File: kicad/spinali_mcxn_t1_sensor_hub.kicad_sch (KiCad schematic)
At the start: 0 parts

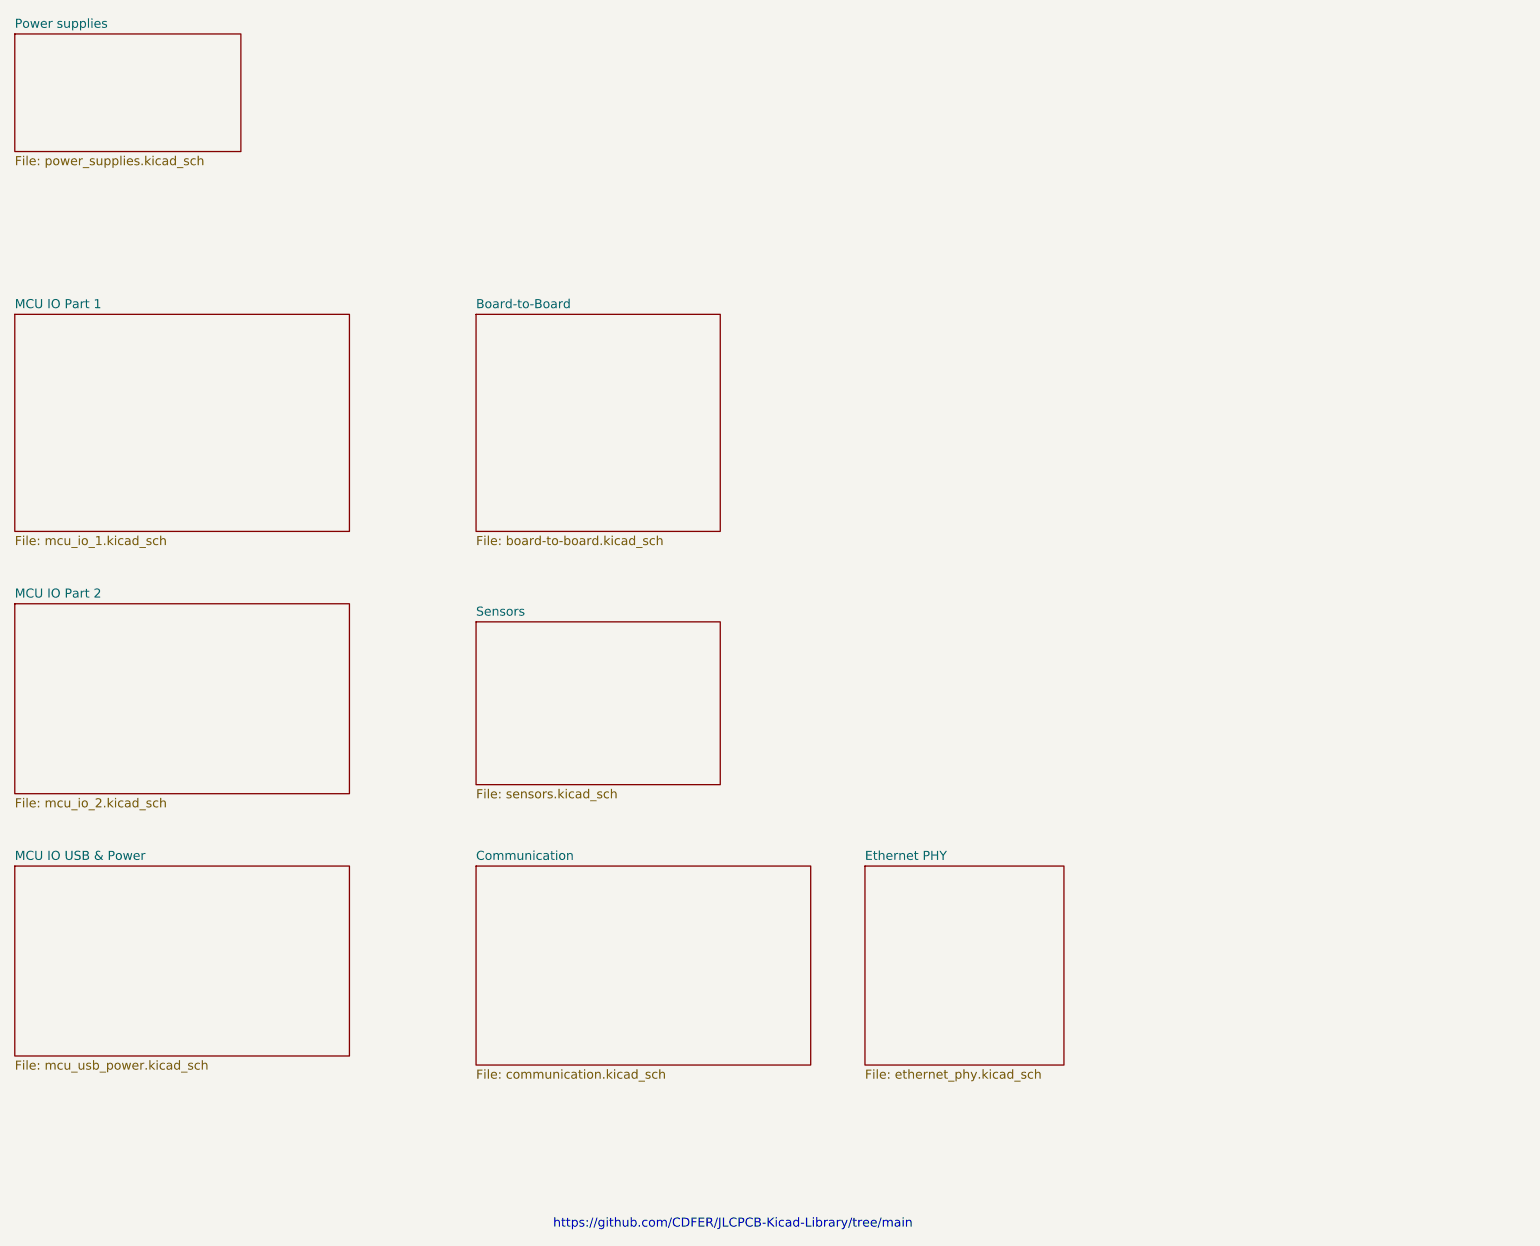
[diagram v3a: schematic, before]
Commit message: Updated schematic after feedback from Jari
- Finished schematic after feedback from Jari. It is at a finished state, can be reviewed by whole team now.
- Layouted MCXN with decoupling caps.
- Layouted Base100-T1 ethernet phy.
- Layouted the power supply a bit.
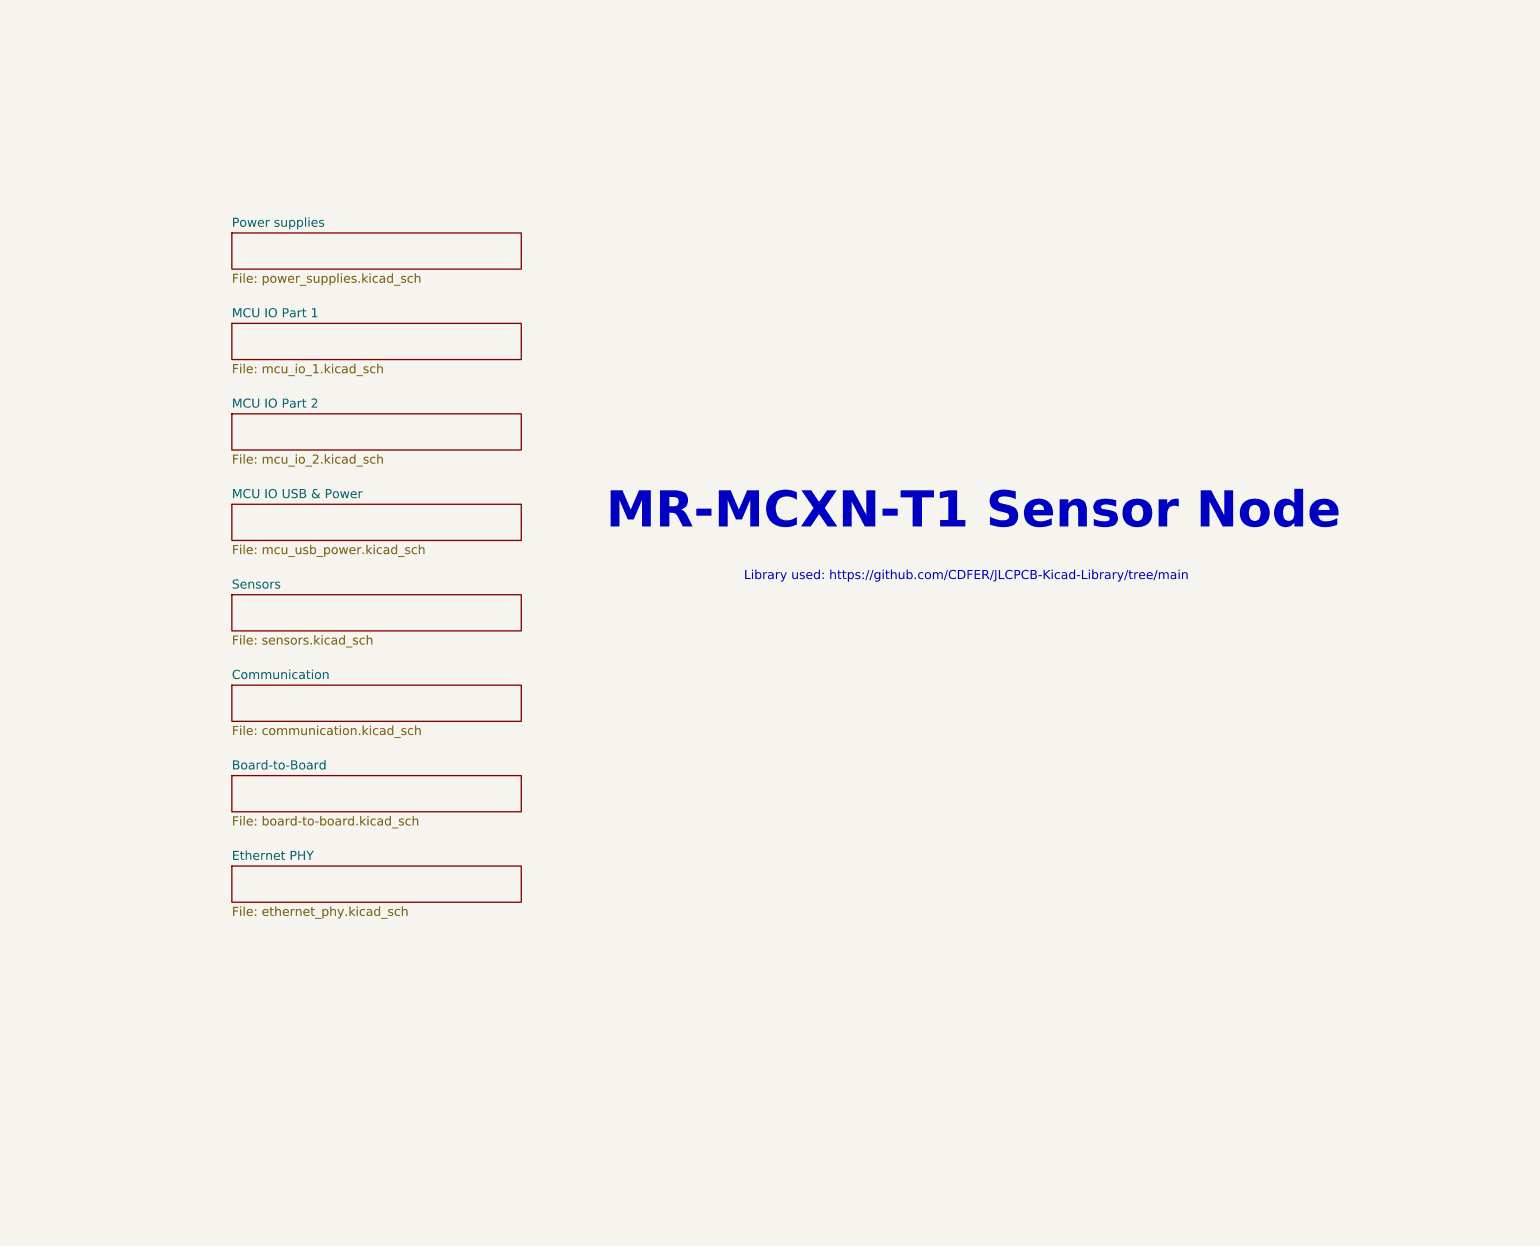
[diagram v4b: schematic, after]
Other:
- note added: "Library used: https://github.com/CDFER/JLCPCB-Kicad-Library/tree/main"
- note added: "MR-MCXN-T1 Sensor Node"
- note removed: "https://github.com/CDFER/JLCPCB-Kicad-Library/tree/main"
- title: MR-MCXN-T1 Sensor hub -> MR-MCXN-T1 Sensor Node
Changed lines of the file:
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@@
 	(paper "A4")
 	(title_block
-		(title "MR-MCXN-T1 Sensor hub")
-		(date "2025-03-20")
+		(title "MR-MCXN-T1 Sensor Node")
+		(date "2025-03-28")
 		(rev "X0")
 		(company "NXP SEMICONDUCTORS B.V.")
@@
 		(comment 4 "CTO SYSTEM INNOVATIONS / MOBILE ROBOTICS DOMAIN")
 	)
-	(text "https://github.com/CDFER/JLCPCB-Kicad-Library/tree/main"
+	(text "MR-MCXN-T1 Sensor Node"
 		(exclude_from_sim no)
-		(at 121.158 191.262 0)
+		(at 154.94 91.186 0)
+		(effects
+			(font
+				(size 5.08 5.08)
+				(thickness 1.016)
+				(bold yes)
+			)
+		)
+	)
+	(text "Library used: https://github.com/CDFER/JLCPCB-Kicad-Library/tree/main"
+		(exclude_from_sim no)
+		(at 153.924 100.33 0)
 		(effects
 			(font
@@
 	)
 	(sheet
-		(at 85.09 63.5)
-		(size 34.29 30.48)
+		(at 50.8 128.27)
+		(size 40.64 5.08)
 		(fields_autoplaced yes)
 		(stroke
@@
 		)
 		(property "Sheetname" "Board-to-Board"
-			(at 85.09 62.7884 0)
+			(at 50.8 127.5584 0)
 			(effects
 				(font
@@
 		)
 		(property "Sheetfile" "board-to-board.kicad_sch"
-			(at 85.09 94.5646 0)
+			(at 50.8 133.9346 0)
 			(effects
 				(font
@@
 	)
 	(sheet
-		(at 20.32 63.5)
-		(size 46.99 30.48)
+		(at 50.8 64.77)
+		(size 40.64 5.08)
 		(fields_autoplaced yes)
 		(stroke
@@
 		)
 		(property "Sheetname" "MCU IO Part 1"
-			(at 20.32 62.7884 0)
+			(at 50.8 64.0584 0)
 			(effects
 				(font
@@
 		)
 		(property "Sheetfile" "mcu_io_1.kicad_sch"
-			(at 20.32 94.5646 0)
+			(at 50.8 70.4346 0)
 			(effects
 				(font
@@
 	)
 	(sheet
-		(at 20.32 104.14)
-		(size 46.99 26.67)
+		(at 50.8 77.47)
+		(size 40.64 5.08)
 		(fields_autoplaced yes)
 		(stroke
@@
 		)
 		(property "Sheetname" "MCU IO Part 2"
-			(at 20.32 103.4284 0)
+			(at 50.8 76.7584 0)
 			(effects
 				(font
@@
 		)
 		(property "Sheetfile" "mcu_io_2.kicad_sch"
-			(at 20.32 131.3946 0)
+			(at 50.8 83.1346 0)
 			(effects
 				(font
@@
 	)
 	(sheet
-		(at 139.7 140.97)
-		(size 27.94 27.94)
+		(at 50.8 140.97)
+		(size 40.64 5.08)
 		(fields_autoplaced yes)
 		(stroke
@@
 		)
 		(property "Sheetname" "Ethernet PHY"
-			(at 139.7 140.2584 0)
+			(at 50.8 140.2584 0)
 			(effects
 				(font
@@
 		)
 		(property "Sheetfile" "ethernet_phy.kicad_sch"
-			(at 139.7 169.4946 0)
+			(at 50.8 146.6346 0)
 			(effects
 				(font
@@
 	)
 	(sheet
-		(at 85.09 106.68)
-		(size 34.29 22.86)
+		(at 50.8 102.87)
+		(size 40.64 5.08)
 		(fields_autoplaced yes)
 		(stroke
@@
 		)
 		(property "Sheetname" "Sensors"
-			(at 85.09 105.9684 0)
+			(at 50.8 102.1584 0)
 			(effects
 				(font
@@
 		)
 		(property "Sheetfile" "sensors.kicad_sch"
-			(at 85.09 130.1246 0)
+			(at 50.8 108.5346 0)
 			(effects
 				(font
@@
 	)
 	(sheet
-		(at 85.09 140.97)
-		(size 46.99 27.94)
+		(at 50.8 115.57)
+		(size 40.64 5.08)
 		(fields_autoplaced yes)
 		(stroke
@@
 		)
 		(property "Sheetname" "Communication"
-			(at 85.09 140.2584 0)
+			(at 50.8 114.8584 0)
 			(effects
 				(font
@@
 		)
 		(property "Sheetfile" "communication.kicad_sch"
-			(at 85.09 169.4946 0)
+			(at 50.8 121.2346 0)
 			(effects
 				(font
@@
 	)
 	(sheet
-		(at 20.32 140.97)
-		(size 46.99 26.67)
+		(at 50.8 90.17)
+		(size 40.64 5.08)
 		(fields_autoplaced yes)
 		(stroke
@@
 		)
 		(property "Sheetname" "MCU IO USB & Power"
-			(at 20.32 140.2584 0)
+			(at 50.8 89.4584 0)
 			(effects
 				(font
@@
 		)
 		(property "Sheetfile" "mcu_usb_power.kicad_sch"
-			(at 20.32 168.2246 0)
+			(at 50.8 95.8346 0)
 			(effects
 				(font
@@
 	)
 	(sheet
-		(at 20.32 24.13)
-		(size 31.75 16.51)
+		(at 50.8 52.07)
+		(size 40.64 5.08)
 		(fields_autoplaced yes)
 		(stroke
@@
 		)
 		(property "Sheetname" "Power supplies"
-			(at 20.32 23.4184 0)
+			(at 50.8 51.3584 0)
 			(effects
 				(font
@@
 		)
 		(property "Sheetfile" "power_supplies.kicad_sch"
-			(at 20.32 41.2246 0)
-			(effects
-				(font
+			(at 50.8 57.7346 0)
+			(effects
+				(font
